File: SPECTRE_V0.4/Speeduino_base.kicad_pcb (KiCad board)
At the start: 2 copper layers, 100 x 93 mm, 185 parts, among them J1 Conn_01x04_Male, J2 Conn_02x04_Odd_Even, J3 Conn_01x06_Male, Q1 2N7002, Q10 BSP78, Q11 BSP78, Q12 BSP78, Q13 BSP78, Q14 BSP78, Q15 BSP78, Q16 BSP78, Q17 BSP78, Q18 BSP78, Q2 CJ2302, Q3 CJ2302, Q4 CJ2302, Q5 BSP78, Q6 BSP78, Q7 CJ2302, Q8 CJ2302, Q9 CJ2302, U1 MAX9926UAEE+, U2 molex_48pin, U3 LM78M05_TO220, U4 MAX3232

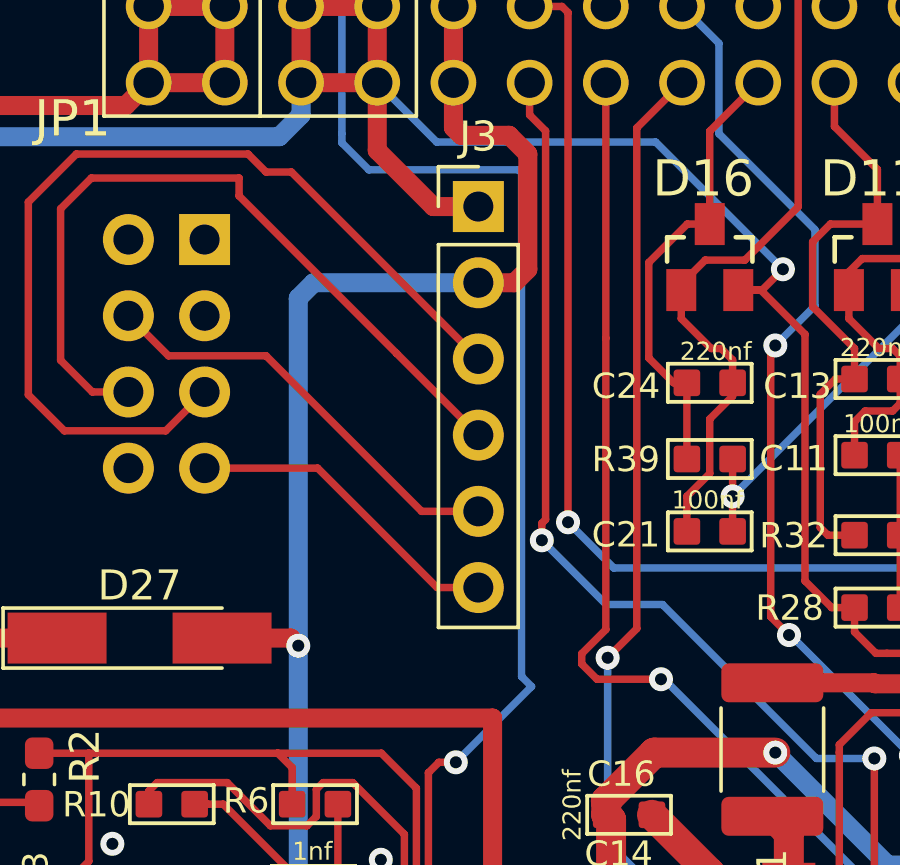
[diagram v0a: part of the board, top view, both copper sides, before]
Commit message: update silkscreen
Updated silkscreen V0.4. Start switchable flyback diode in V0.5 for PWM control of injectors
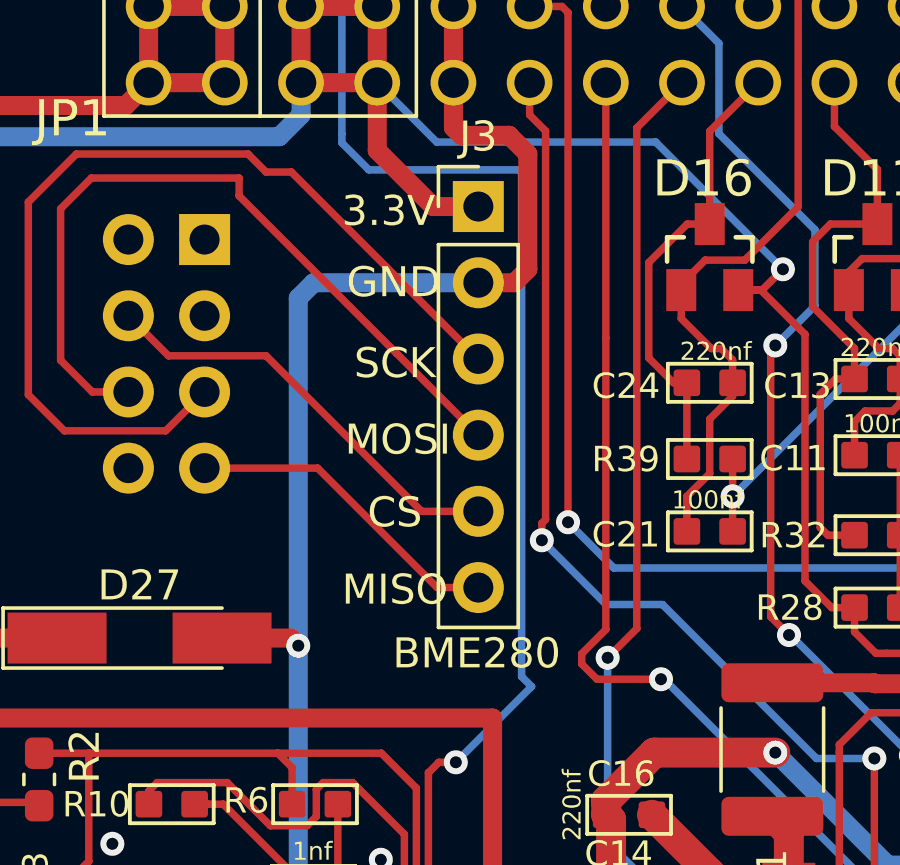
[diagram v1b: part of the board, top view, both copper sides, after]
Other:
- board text added: "BME280"
- board text added: "CS"
- board text added: "MISO"
- board text added: "MOSI"
- board text added: "SCK"
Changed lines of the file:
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@@
   (general
     (thickness 1.6)
-    (drawings 37)
+    (drawings 44)
     (tracks 2570)
     (zones 0)
@@
     )
   )
+  (gr_text BME280 (at 135.993 50.297) (layer F.SilkS)
+    (effects (font (size 1 1) (thickness 0.15)))
+  )
+  (gr_text MISO (at 133.268 48.172) (layer F.SilkS)
+    (effects (font (size 1 1) (thickness 0.15)))
+  )
+  (gr_text CS (at 133.268 45.597) (layer F.SilkS)
+    (effects (font (size 1 1) (thickness 0.15)))
+  )
+  (gr_text MOSI (at 133.368 43.172) (layer F.SilkS)
+    (effects (font (size 1 1) (thickness 0.15)))
+  )
+  (gr_text SCK (at 133.268 40.622) (layer F.SilkS)
+    (effects (font (size 1 1) (thickness 0.15)))
+  )
+  (gr_text GND (at 133.225 37.925) (layer F.SilkS)
+    (effects (font (size 1 1) (thickness 0.15)))
+  )
+  (gr_text 3.3V (at 133.05 35.55) (layer F.SilkS)
+    (effects (font (size 1 1) (thickness 0.15)))
+  )
   (gr_arc (start 114.25 109.75) (end 114 109.75) (angle -90) (layer Edge.Cuts) (width 0.05))
